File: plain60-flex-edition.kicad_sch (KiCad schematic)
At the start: 173 parts, among them J1 HRO-TYPE-C-31-M-12, J2 ISP, J3 ai03_ud, K1 KEYSW, K10 KEYSW, K11 KEYSW, K12 KEYSW, K13 KEYSW, K14 KEYSW, K15 KEYSW, K15-1 KEYSW, K16 KEYSW, K17 KEYSW, K18 KEYSW, K19 KEYSW, K2 KEYSW, K20 KEYSW, K21 KEYSW, K22 KEYSW, K23 KEYSW, K24 KEYSW, K25 KEYSW, K26 KEYSW, K27 KEYSW, K28 KEYSW, K29 KEYSW, K3 KEYSW, K31 KEYSW, K31-1 KEYSW, K32 KEYSW, K33 KEYSW, K34 KEYSW, K35 KEYSW, K36 KEYSW, K37 KEYSW, K38 KEYSW, K39 KEYSW, K4 KEYSW, K40 KEYSW, K41 KEYSW, K42 KEYSW, K43 KEYSW, K44 KEYSW, K44-1 KEYSW, K46 KEYSW, K46-1 KEYSW, K47 KEYSW, K48 KEYSW, K49 KEYSW, K5 KEYSW, K50 KEYSW, K51 KEYSW, K52 KEYSW, K53 KEYSW, K54 KEYSW, K55 KEYSW, K56 KEYSW, K57 KEYSW, K58 KEYSW, K58-1 KEYSW, K59 KEYSW, K6 KEYSW, K61 KEYSW, K61-1 KEYSW, K62 KEYSW, K62-1 KEYSW, K63 KEYSW, K63-1 KEYSW, K67 KEYSW, K67-1 KEYSW, K7 KEYSW, K71 KEYSW, K72 KEYSW, K72-1 KEYSW, K73 KEYSW, K73-1 KEYSW, K74 KEYSW, K74-1 KEYSW, K8 KEYSW, K9 KEYSW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

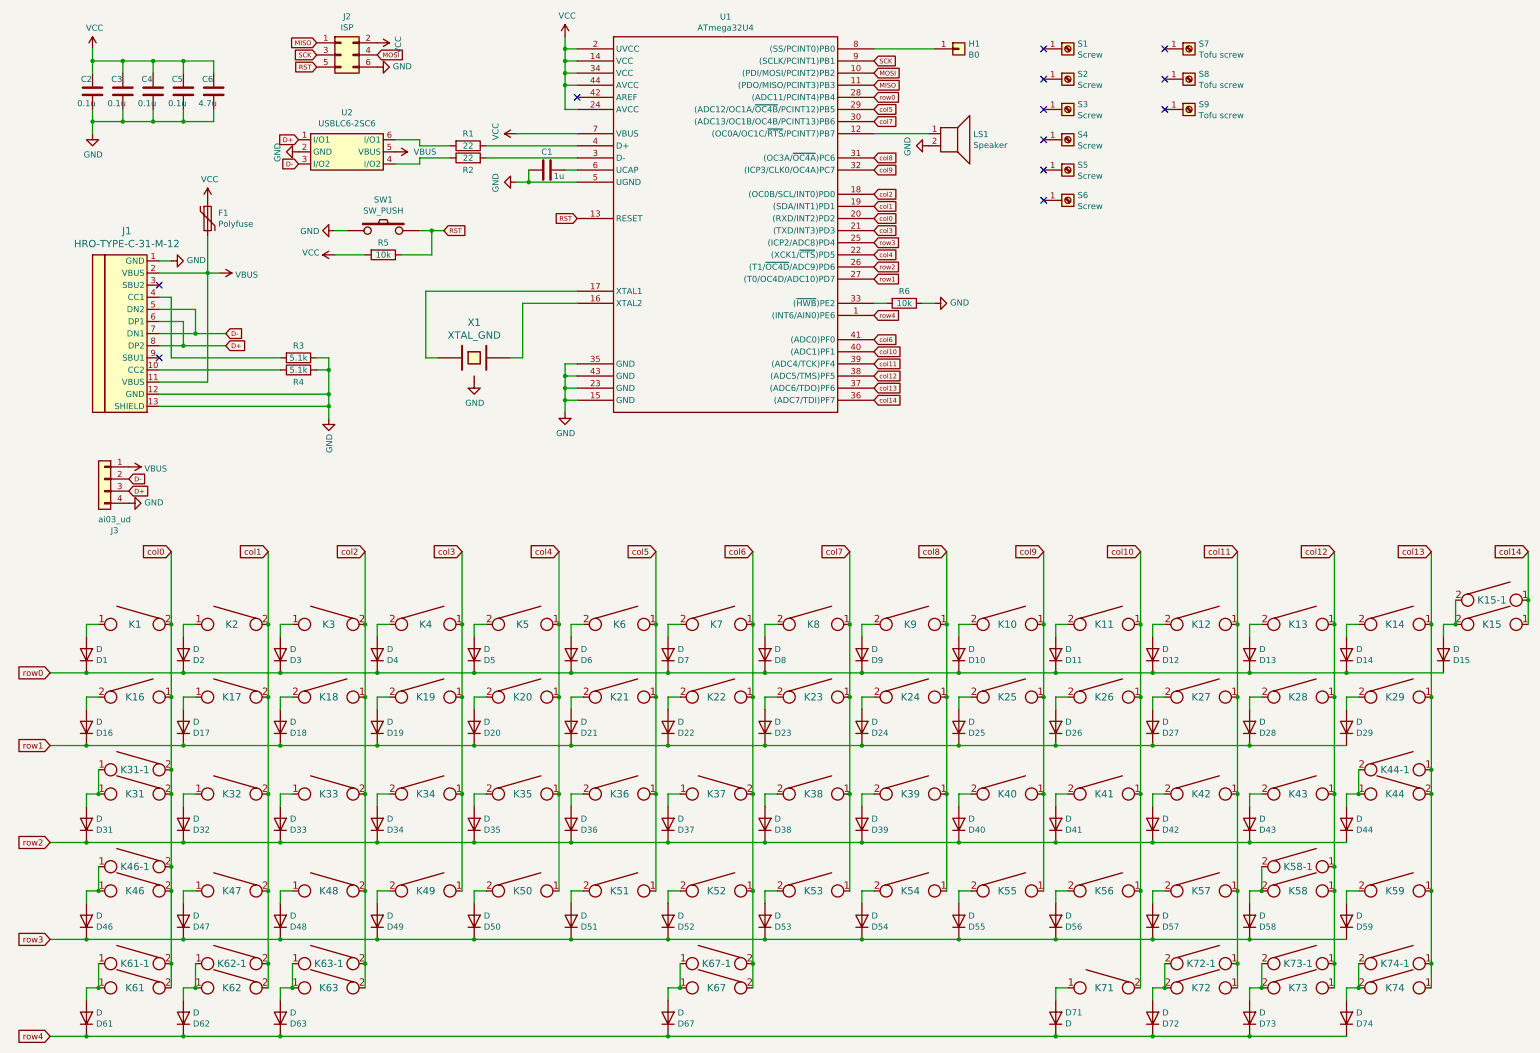
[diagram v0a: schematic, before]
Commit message: Change footprints to MX+ALPS
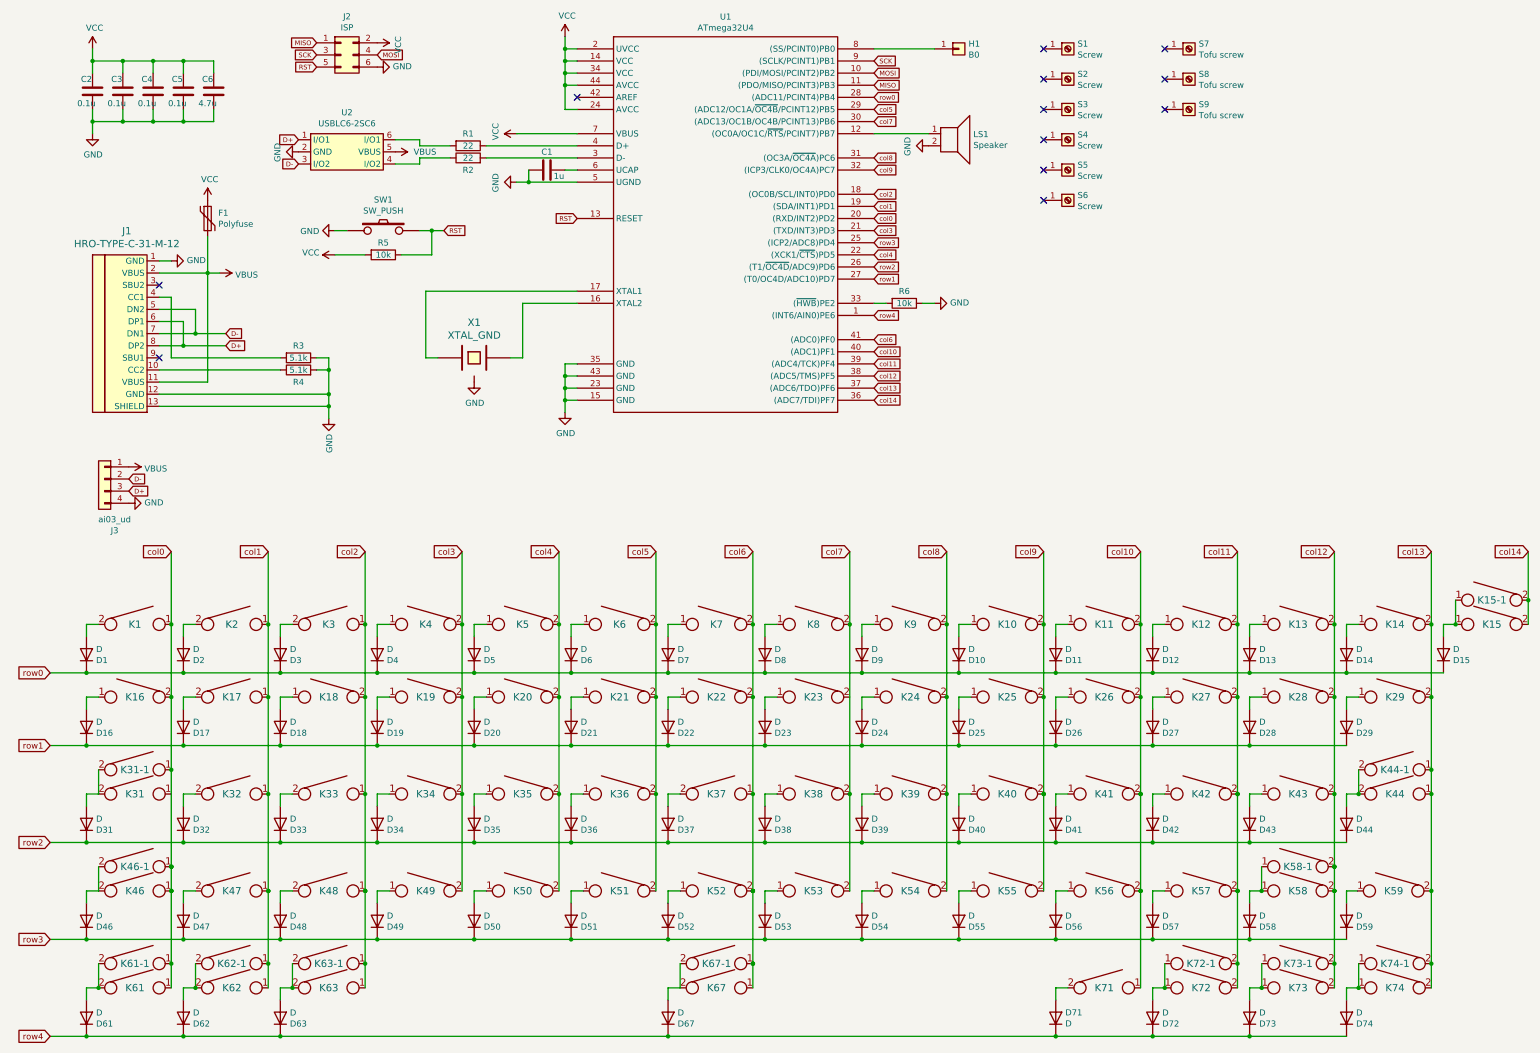
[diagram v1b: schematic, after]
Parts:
- K1, K10, K11, K12, K13, K14, K15-1, K17, K18, K19, K2, K20, K21, K22, K23, K24, K25, K26, K27, K28, K3, K32, K33, K34, K35, K36, K37, K38, K39, K4, K40, K41, K42, K47, K48, K49, K5, K50, K51, K52, K53, K54, K55, K56, K57, K59, K6, K62-1, K7, K73-1, K8, K9: footprint Keeb_switches:CHERRY_PLATE_100H -> MX_Alps_Hybrid:MX-1U-NoLED
- K15: footprint Keeb_switches:CHERRY_PCB_200H -> MX_Alps_Hybrid:MX-2U-NoLED
- K16, K29, K61-1, K63-1, K72-1, K74-1: footprint Keeb_switches:CHERRY_PLATE_150H -> MX_Alps_Hybrid:MX-1.5U-NoLED
- K31, K58-1: footprint Keeb_switches:CHERRY_PLATE_175H -> MX_Alps_Hybrid:MX-1.75U-NoLED
- K31-1, K46-1, K61, K62, K63, K71, K72, K73, K74: footprint Keeb_switches:CHERRY_PLATE_125H -> MX_Alps_Hybrid:MX-1.25U-NoLED
- K43: footprint Keeb_switches:CHERRY_PLATE_100H -> MX_Alps_Hybrid:MX-1.5U-NoLED
- K44: footprint Keeb_switches:CHERRY_PCB_225H_F -> MX_Alps_Hybrid:MX-2.25U-NoLED
- K44-1: footprint Keeb_switches:CHERRY_PCB_200H_V -> MX_Alps_Hybrid:MX-ISO-FLIPPED-ReversedStabilizers
- K46: footprint Keeb_switches:CHERRY_PCB_225H -> MX_Alps_Hybrid:MX-2.25U-NoLED
- K58: footprint Keeb_switches:CHERRY_PCB_275H -> MX_Alps_Hybrid:MX-2.75U-NoLED
- K67: footprint Keeb_switches:CHERRY_PCB_625H_F -> MX_Alps_Hybrid:MX-6.25U-ReversedStabilizers-NoLED
- K67-1: footprint Keeb_switches:CHERRY_PCB_700H_F -> MX_Alps_Hybrid:MX-7U-ReversedStabilizers-NoLED
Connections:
- net col0: now also K1.1, K16.2, K31-1.1, K46-1.1, K46.1, K61-1.1, K61.1; no longer K1.2, K16.1, K31-1.2, K31.2, K46-1.2, K46.2, K61-1.2, K61.2
- net col1: now also K17.1, K2.1, K32.1, K47.1, K62-1.1, K62.1; no longer K17.2, K2.2, K32.2, K47.2, K62-1.2, K62.2
- net col10: now also K11.2, K26.2, K41.2, K56.2, K71.1; no longer K11.1, K26.1, K41.1, K56.1, K71.2
- net col11: now also K12.2, K27.2, K42.2, K57.2, K72-1.2, K72.2; no longer K12.1, K27.1, K42.1, K57.1, K72-1.1, K72.1
- net col12: now also K13.2, K28.2, K43.2, K58-1.2, K58.2, K73-1.2, K73.2; no longer K13.1, K28.1, K43.1, K58-1.1, K58.1, K73-1.1, K73.1
- net col13: now also K14.2, K29.2, K44.1, K59.2, K74-1.2, K74.2; no longer K14.1, K29.1, K44.2, K59.1, K74-1.1, K74.1
- net col14: now also K15-1.2, K15.2; no longer K15-1.1, K15.1
- net col2: now also K18.2, K3.1, K33.1, K48.1, K63-1.1, K63.1; no longer K18.1, K3.2, K33.2, K48.2, K63-1.2, K63.2
- net col3: now also K19.2, K34.2, K4.2, K49.2; no longer K19.1, K34.1, K4.1, K49.1
- net col4: now also K20.2, K35.2, K5.2, K50.2; no longer K20.1, K35.1, K5.1, K50.1
- net col5: now also K21.2, K36.2, K51.2, K6.2; no longer K21.1, K36.1, K51.1, K6.1
- net col6: now also K22.2, K37.1, K52.2, K67-1.1, K67.1, K7.2; no longer K22.1, K37.2, K52.1, K67-1.2, K67.2, K7.1
- net col7: now also K38.2, K53.2, K8.2; no longer K23.1, K38.1, K53.1, K8.1
- net col8: now also K24.2, K39.2, K54.2, K9.2; no longer K24.1, K39.1, K54.1, K9.1
- net col9: now also K10.2, K25.2, K40.2, K55.2; no longer K10.1, K25.1, K40.1, K55.1
- net at D1.2 (A): now also K1.2; no longer K1.1
- net at D2.2 (A): now also K2.2; no longer K2.1
- net at D3.2 (A): now also K3.2; no longer K3.1
- net at D4.2 (A): now also K4.1; no longer K4.2
- net at D5.2 (A): now also K5.1; no longer K5.2
- net at D6.2 (A): now also K6.1; no longer K6.2
- net at D7.2 (A): now also K7.1; no longer K7.2
- net at D8.2 (A): now also K8.1; no longer K8.2
- net at D9.2 (A): now also K9.1; no longer K9.2
- net at D10.2 (A): now also K10.1; no longer K10.2
- net at D11.2 (A): now also K11.1; no longer K11.2
- net at D12.2 (A): now also K12.1; no longer K12.2
- net at D13.2 (A): now also K13.1; no longer K13.2
- net at D14.2 (A): now also K14.1; no longer K14.2
- net at D16.2 (A): now also K16.1; no longer K16.2
- net at D17.2 (A): now also K17.2; no longer K17.1
- net at D18.2 (A): now also K18.1; no longer K18.2
- net at D19.2 (A): now also K19.1; no longer K19.2
- net at D20.2 (A): now also K20.1; no longer K20.2
- net at D21.2 (A): now also K21.1; no longer K21.2
- net at D22.2 (A): now also K22.1; no longer K22.2
- net at D23.2 (A): now also K23.1; no longer K23.2
- net at D24.2 (A): now also K24.1; no longer K24.2
- net at D25.2 (A): now also K25.1; no longer K25.2
- net at D26.2 (A): now also K26.1; no longer K26.2
- net at D27.2 (A): now also K27.1; no longer K27.2
- net at D28.2 (A): now also K28.1; no longer K28.2
- net at D29.2 (A): now also K29.1; no longer K29.2
- net at D32.2 (A): now also K32.2; no longer K32.1
- net at D33.2 (A): now also K33.2; no longer K33.1
- net at D34.2 (A): now also K34.1; no longer K34.2
- net at D35.2 (A): now also K35.1; no longer K35.2
- net at D36.2 (A): now also K36.1; no longer K36.2
- net at D37.2 (A): now also K37.2; no longer K37.1
- net at D38.2 (A): now also K38.1; no longer K38.2
- net at D39.2 (A): now also K39.1; no longer K39.2
- net at D40.2 (A): now also K40.1; no longer K40.2
- net at D41.2 (A): now also K41.1; no longer K41.2
- net at D42.2 (A): now also K42.1; no longer K42.2
- net at D43.2 (A): now also K43.1; no longer K43.2
- net at D44.2 (A), K44-1.2: now also K44.2; no longer K44.1
- net at D47.2 (A): now also K47.2; no longer K47.1
- net at D48.2 (A): now also K48.2; no longer K48.1
- net at D49.2 (A): now also K49.1; no longer K49.2
- net at D50.2 (A): now also K50.1; no longer K50.2
- net at D51.2 (A): now also K51.1; no longer K51.2
- net at D52.2 (A): now also K52.1; no longer K52.2
- net at D53.2 (A): now also K53.1; no longer K53.2
- net at D54.2 (A): now also K54.1; no longer K54.2
- net at D55.2 (A): now also K55.1; no longer K55.2
- net at D56.2 (A): now also K56.1; no longer K56.2
- net at D57.2 (A): now also K57.1; no longer K57.2
- net at D59.2 (A): now also K59.1; no longer K59.2
- net at D71.2 (A): now also K71.2; no longer K71.1
- new net: D15.2 (A), K15-1.1, K15.1
- new net: D31.2 (A), K31-1.2, K31.2
- new net: D46.2 (A), K46-1.2, K46.2
- new net: D58.2 (A), K58-1.1, K58.1
- new net: D61.2 (A), K61-1.2, K61.2
- new net: D62.2 (A), K62-1.2, K62.2
- new net: D63.2 (A), K63-1.2, K63.2
- new net: D67.2 (A), K67-1.2, K67.2
- new net: D72.2 (A), K72-1.1, K72.1
- new net: D73.2 (A), K73-1.1, K73.1
- new net: D74.2 (A), K74-1.1, K74.1
- now unconnected: K31.1

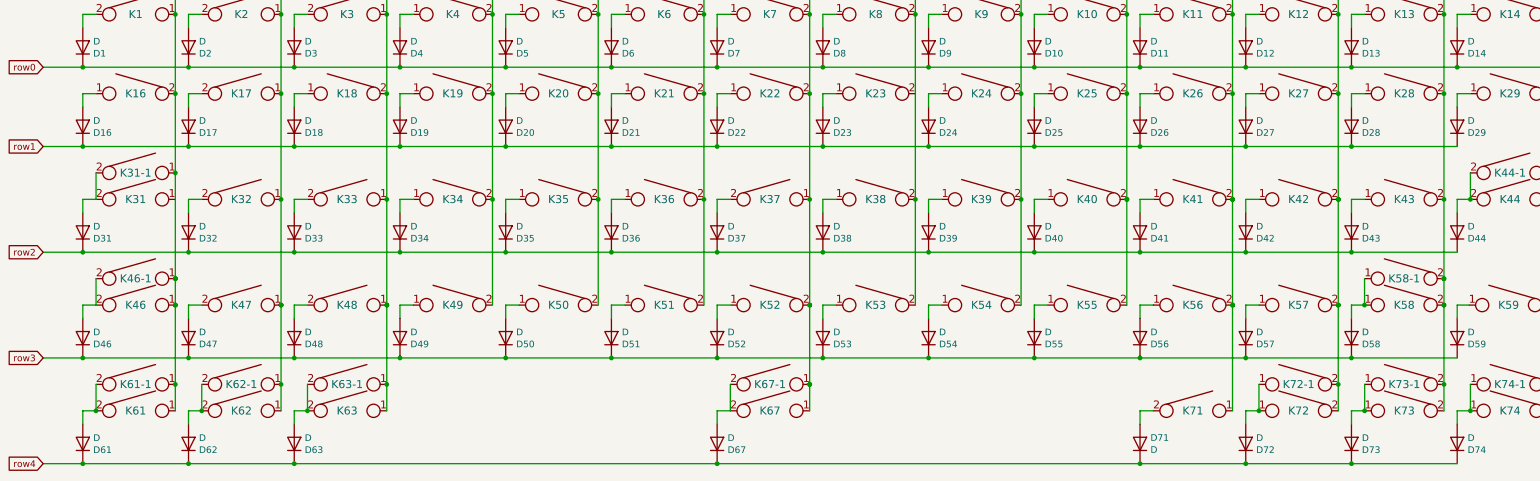
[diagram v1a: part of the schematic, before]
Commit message: Add AEK support
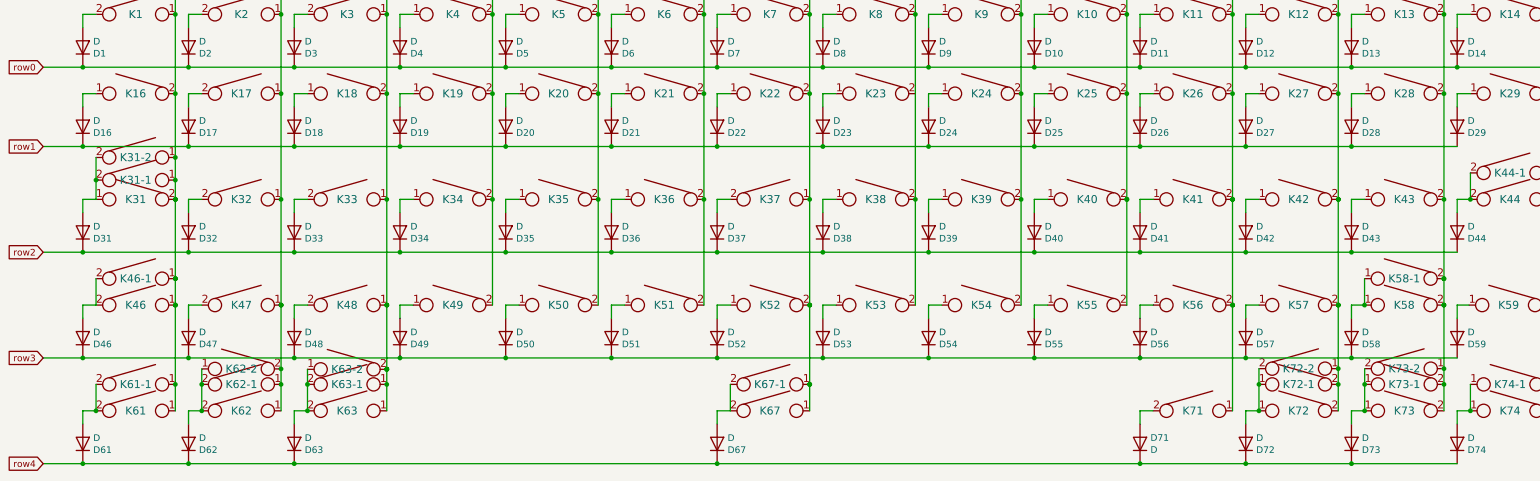
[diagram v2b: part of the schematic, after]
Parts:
- added K31-2, K63-2, K72-2: KEYSW, Alps_Only:ALPS-1.5U, symbol keyboard_parts:KEYSW
- added K62-2, K73-2: KEYSW, Alps_Only:ALPS-1.25U, symbol keyboard_parts:KEYSW
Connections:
- net col0: now also K31.2, K31-2.1
- net col1: now also K62-2.2
- net col11: now also K72-2.1
- net col12: now also K73-2.1
- net col2: now also K63-2.2
- net at K31.1: now also D31.2 (A), K31-1.2, K31-2.2
- net at D62.2 (A), K62-1.2, K62.2: now also K62-2.1
- net at D63.2 (A), K63-1.2, K63.2: now also K63-2.1
- net at D72.2 (A), K72-1.1, K72.1: now also K72-2.2
- net at D73.2 (A), K73-1.1, K73.1: now also K73-2.2
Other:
- moved on the sheet: K31-1
